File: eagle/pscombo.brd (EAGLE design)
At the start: 128.5 x 101.9 mm, 14 parts

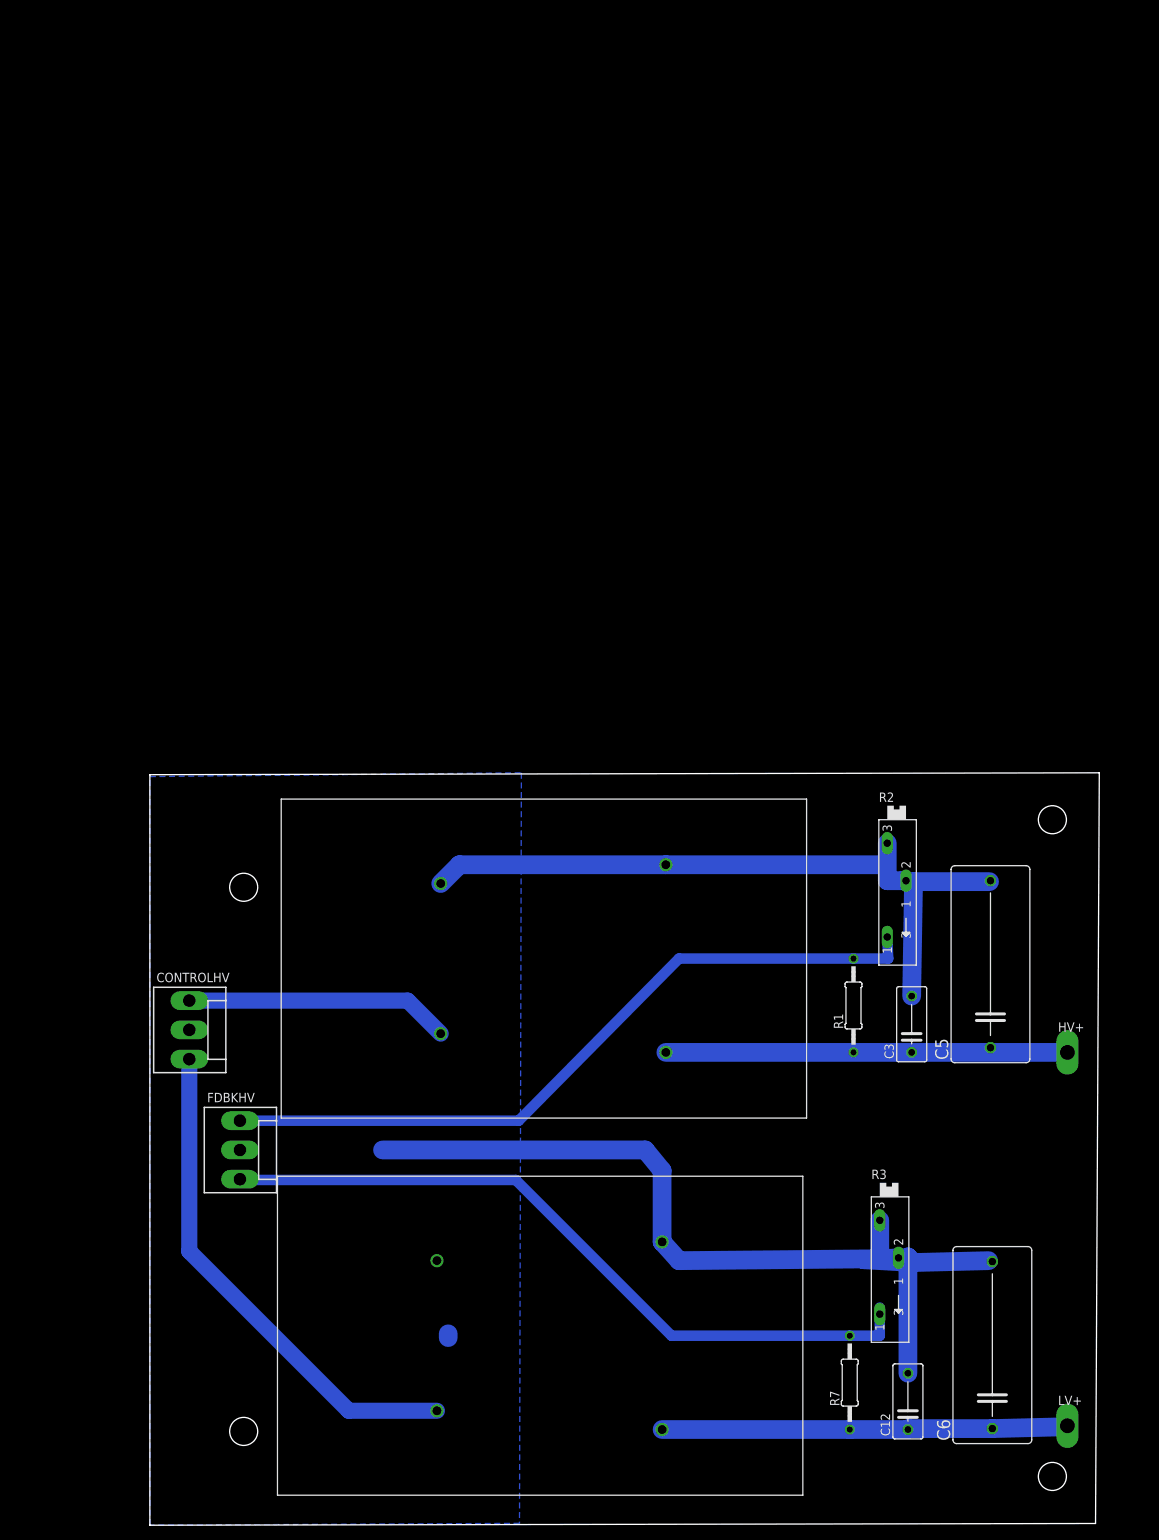
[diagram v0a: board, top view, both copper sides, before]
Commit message: 3PS, 2 1kV in parallel
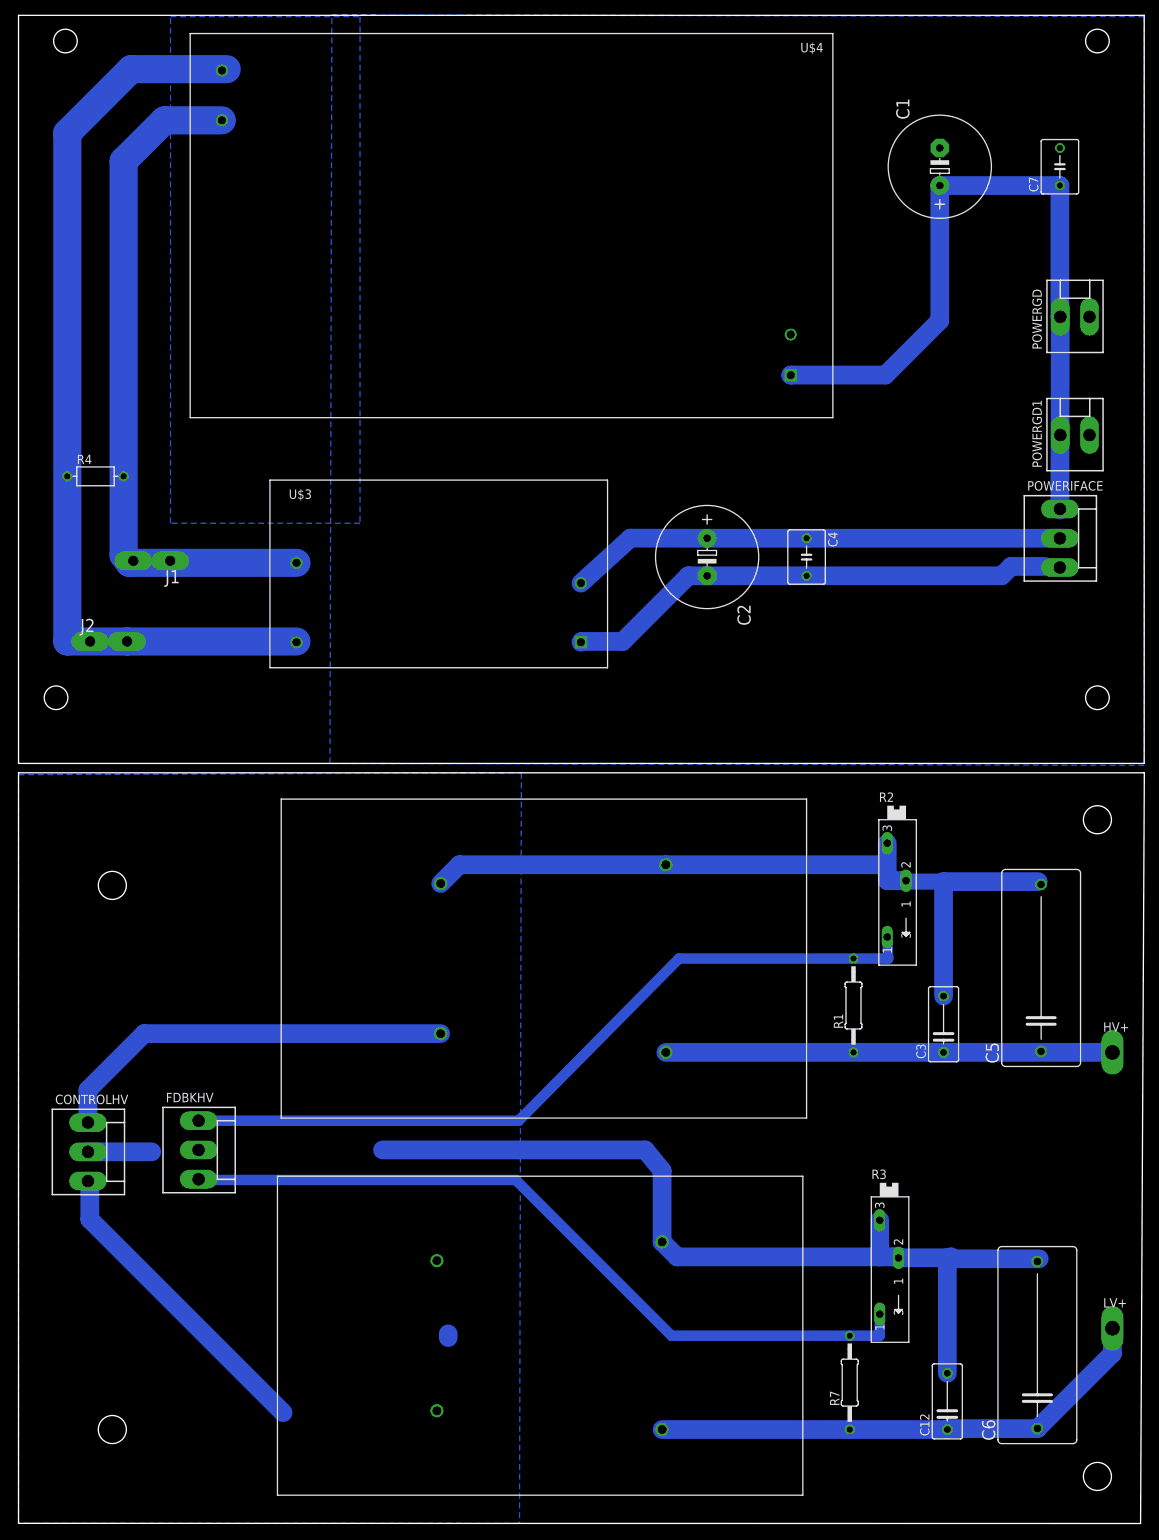
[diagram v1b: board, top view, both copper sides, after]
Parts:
- added C1, C2: (no value), rcl:E5-13
- added C4, C7: (no value), rcl:C050-050X075
- added J1, J2: PIN2F061.100, con-faston:F061.100
- added POWERGD, POWERGD1: (no value), con-molex:KK-156-2
- added POWERIFACE: (no value), con-molex:KK-156-3
- added R4: VARISTOR-7,5, varistor:R-7,5
- added U$3: IRM-05-05, meanwell:IRM-05-05
- added U$4: IRM-60-12, meanwell:IRM-60-12
- moved CONTROLHV 21.5 mm to (9.40, 50.3)
- moved LV+ 14.5 mm to (148.1, 26.4)
- moved C5 6.88 mm to (138.4, 75.2)
- moved C6 6.10 mm to (137.9, 24.1)
- moved HV+ 6.10 mm to (148.1, 63.8)
- moved FDBKHV 5.59 mm to (24.4, 50.5)
- moved C12 5.33 mm to (125.7, 16.5)
- moved C3 4.32 mm to (125.2, 67.6)
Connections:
- new net +15V: C1.+, C7.1, POWERGD.1, POWERGD1.1, POWERIFACE.1, U$4.P$1
- new net GND1: C1.-, C2.-, C4.2, C7.2, POWERGD.2, POWERGD1.2, POWERIFACE.3, U$3.-V, U$4.P$2
- new net N$6: J1.A1, J1.A2, R4.2, U$3.ACN, U$4.P$4
- new net N$7: J2.A1, J2.A2, R4.1, U$3.ACL, U$4.P$3
- new net VCC: C2.+, C4.1, POWERIFACE.2, U$3.+V
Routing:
- net N$7: track 0.00 -> 125.0 mm
- net +15V: track 0.00 -> 101.8 mm
- net N$6: track 0.00 -> 92.9 mm
- net GND1: track 0.00 -> 67.4 mm
- net VCC: track 0.00 -> 67.2 mm
- net N$5: track 68.5 -> 42.3 mm
- net N$4: track 35.9 -> 55.3 mm
- net N$2: track 55.0 -> 68.7 mm
- net GND: track 222.6 -> 234.5 mm
- net N$8: track 99.5 -> 105.6 mm
- net N$1: track 54.4 -> 60.5 mm
- net N$3: track 99.8 -> 105.4 mm
- added copper zone on layer 16, net GND1
- added copper zone on layer 16, net N$9
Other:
- board size 128.5 x 101.9 mm -> 152.4 x 204.2 mm

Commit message: capacitor bank
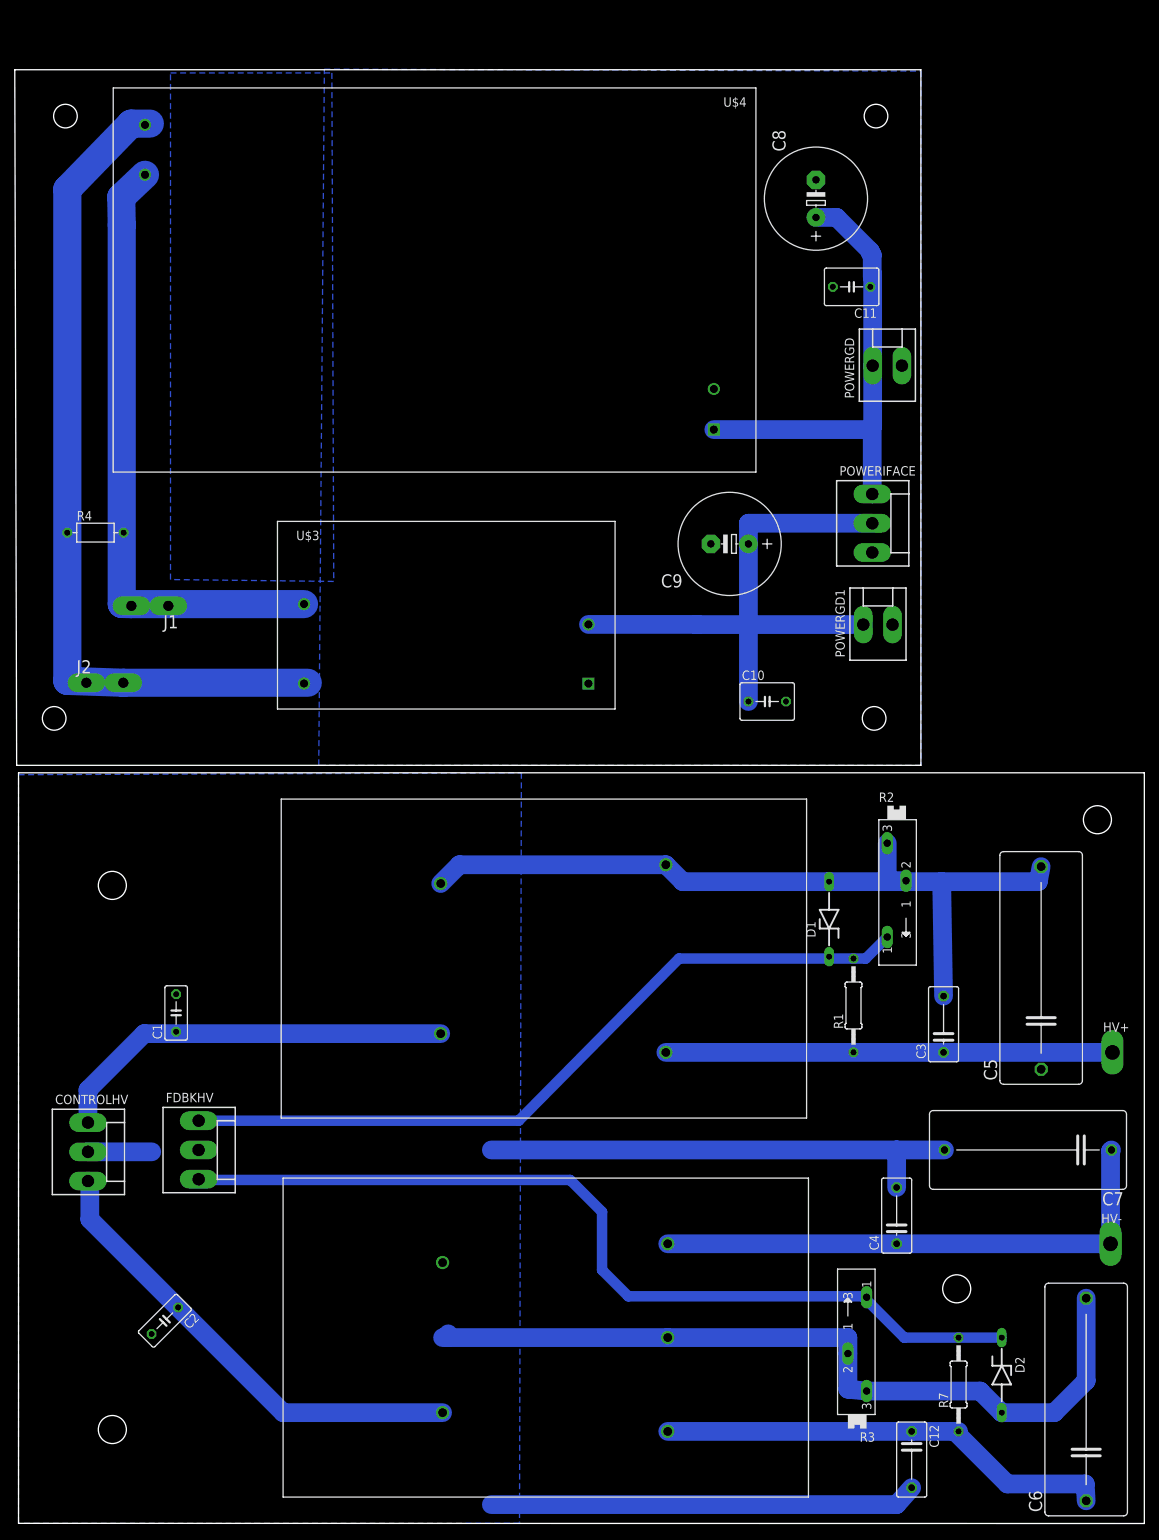
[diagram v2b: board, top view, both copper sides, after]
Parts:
- removed LV+: TPPAD1-20Y, testpad:P1-20Y
- added C10, C11: (no value), rcl:C050-050X075
- added C8, C9: (no value), rcl:E5-13
- added D1, D2: 1n4733, diode:ZDIO-10
- added HV-: TPPAD1-20Y, testpad:P1-20Y
- C1, C2: device rcl:E5-13 -> rcl:C050-030X075
- C4: value (none) -> .01u; device rcl:C050-050X075 -> rcl:C075-042X103
- C5, C6: device rcl:C225-108X268 -> rcl:C275-113X316
- C7: value (none) -> 1u; device rcl:C050-050X075 -> rcl:C225-108X268
- U$2: value EMCO-F104PIN -> EMCO-F20CT; device dc-dc-converter:EMCO-F -> dc-dc-converter:EMCO-F*CT
- moved C1 154.3 mm to (21.3, 69.1)
- moved C7 133.2 mm to (136.7, 50.5), turned to 180 degrees
- moved C2 126.8 mm to (19.8, 27.4), turned to 225 degrees
- moved C4 90.0 mm to (118.9, 41.7), turned to 90 degrees
- moved POWERGD1 37.0 mm to (116.3, 121.7)
- moved POWERGD 26.2 mm to (117.6, 156.7)
- moved POWERIFACE 25.5 mm to (115.6, 135.4)
- moved R7 14.7 mm to (127.3, 18.8)
- moved U$4 12.8 mm to (99.8, 194.3)
- moved R3 10.1 mm to (113.5, 24.9), turned to 90 degrees
- moved C6 9.89 mm to (144.5, 16.8)
- moved C12 9.24 mm to (120.9, 8.64), turned to 270 degrees
- moved R4 7.62 mm to (10.4, 134.1)
- moved J1 6.10 mm to (17.8, 124.2)
- moved U$3 5.68 mm to (35.1, 110.2)
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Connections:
- removed net +15V: C1.+, C7.1, POWERGD.1, POWERGD1.1, POWERIFACE.1, U$4.P$1
- new net +12V: C11.1, C8.+, POWERGD.1, POWERIFACE.1, U$4.P$1
- new net N$6: C4.1, C7.1, HV-.TP, U$2.P$4
- net GND: now also C1.2, C2.2, C4.2, C7.2, D1.A, D2.A, U$2.P$5; no longer U$2.P$4
- net GND1: now also C10.2, C11.2, C8.-, C9.-; no longer C1.-, C2.-, C4.2, C7.2
- net N$2: no longer LV+.TP
- net N$3: now also D1.C
- net N$4: now also C1.1
- net N$5: now also C2.1
- net N$8: now also D2.C
- net VCC: now also C10.1, C9.+, POWERGD1.1; no longer C2.+, C4.1
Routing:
- net GND: track 234.5 -> 349.9 mm
- net +15V: track 101.8 -> 0.00 mm
- net N$6: track 0.00 -> 72.7 mm
- net GND1: track 67.4 -> 0.00 mm
- net +12V: track 0.00 -> 64.5 mm
- net N$5: track 42.3 -> 63.9 mm
- net N$8: track 105.6 -> 122.2 mm
- net VCC: track 67.2 -> 78.6 mm
- net N$9: track 125.0 -> 114.0 mm
- net N$7: track 92.9 -> 84.2 mm
- net N$2: track 68.7 -> 62.3 mm
- net N$3: track 105.4 -> 103.6 mm
- added copper zone on layer 16, net N$10
- removed copper zone on layer 16, net N$9 (its old number)
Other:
- board size 152.4 x 204.2 mm -> 152.9 x 196.8 mm

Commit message: IXYS board solution, gatedriver components
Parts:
- removed HV-: TPPAD1-20Y, testpad:P1-20Y
- added LV+: TPPAD1-20Y, testpad:P1-20Y
- C1: value (none) -> 1n; device rcl:C050-030X075 -> rcl:C075-042X103
- C2: value (none) -> 10p; device rcl:C050-030X075 -> rcl:C075-042X103
- C4: value .01u -> 1n
- C5, C6: device rcl:C275-113X316 -> rcl:C275-205X316
- C7: value 1u -> 10p; device rcl:C225-108X268 -> rcl:C075-042X103
- D1, D2: value 1n4733 -> 1N4004; device diode:ZDIO-10 -> diode:DO41-10
- U$2: value EMCO-F20CT -> EMCO-F104PIN; device dc-dc-converter:EMCO-F*CT -> dc-dc-converter:EMCO-F
- moved C2 88.9 mm to (99.1, 67.8), turned to 90 degrees
- moved C1 82.8 mm to (104.1, 67.8)
- moved C7 41.9 mm to (104.1, 24.1), turned to 90 degrees
- moved R7 35.7 mm to (92.5, 26.7)
- moved R3 27.9 mm to (95.2, 46.0), turned to 270 degrees
- moved C6 27.5 mm to (123.2, 34.0)
- moved D1 27.3 mm to (119.6, 56.4), turned to 180 degrees
- moved C12 27.2 mm to (98.6, 24.1), turned to 90 degrees
- moved R1 20.1 mm to (93.0, 70.6)
- moved C4 19.5 mm to (110.2, 24.1)
- moved R2 18.1 mm to (101.3, 89.4)
- moved CONTROLHV 17.5 mm to (5.33, 67.3)
- moved U$2 17.0 mm to (40.4, 15.7)
- moved U$1 16.8 mm to (40.4, 66.8)
- moved HV+ 16.2 mm to (133.6, 56.4), turned to 90 degrees
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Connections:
- new net N$7: D2.C, LV+.TP
- net GND: now also U$2.P$4; no longer D1.A, D2.A, U$2.P$5
- net N$1: now also C1.1, C2.1, D1.A; no longer HV+.TP
- net N$2: now also C4.1, C7.1, D2.A
- net N$3: no longer D1.C
- net N$4: no longer C1.1
- net N$5: no longer C2.1
- net N$6: now also D1.C, HV+.TP; no longer C4.1, C7.1, HV-.TP, U$2.P$4
- net N$8: no longer D2.C
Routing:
- net GND: track 349.9 -> 267.2 mm
- net N$6: track 72.7 -> 10.2 mm
- net N$8: track 122.2 -> 95.1 mm
- net N$4: track 55.3 -> 37.2 mm
- net N$7: track 0.00 -> 10.8 mm
- net N$5: track 63.9 -> 70.0 mm
- net N$2: track 62.3 -> 64.5 mm
- net N$1: track 60.5 -> 61.0 mm
- added copper zone on layer 16, net N$11
- removed copper zone on layer 16, net N$10 (its old number)
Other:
- board size 152.9 x 196.8 mm -> 137.9 x 196.5 mm
